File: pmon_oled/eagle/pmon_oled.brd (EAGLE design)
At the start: 60 x 60 mm, 37 parts, among them J1 USB, J2 USB, J4 PINHD-1X3, J5 PINHD-2X3, Q1 16Mhz, U1 LTC2943, U2 FT232RL, U3 LT1764AEQ, U4 ATMEGA328TQFP32

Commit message: Minor board tweaks. Ready for final auto routing.
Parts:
- moved J5 0.48 mm to (4.12, 26.7)
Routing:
- net +5V: track 160.2 -> 161.1 mm
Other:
- board text added: "(+)"
- board text added: "(-)"
- board text added: "(3.8V)"
- board text added: "+5V"
- board text added: "ICSP"
- board text added: "MODE"
- board text added: "POWER"
- board text added: "POWER-PLAY OLED - REV A OSH GITHUB"
- board text added: "POWER-PLAY OLED Rev A, May 2014 Single-Cell Power Monitor. Github OSH"
- board text added: "USB"
- board text added: "VOUT"
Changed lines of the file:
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@@
 <setting verticaltext="up"/>
 </settings>
-<grid distance="25" unitdist="mil" unit="mm" style="lines" multiple="1" display="yes" altdistance="0.000123031496" altunitdist="mil" altunit="mil"/>
+<grid distance="25" unitdist="mil" unit="mil" style="lines" multiple="1" display="yes" altdistance="0.000123031496" altunitdist="mil" altunit="mil"/>
 <layers>
 <layer number="1" name="Top" color="4" fill="1" visible="yes" active="yes"/>
@@
 <layer number="19" name="Unrouted" color="6" fill="1" visible="yes" active="yes"/>
 <layer number="20" name="Dimension" color="15" fill="1" visible="yes" active="yes"/>
-<layer number="21" name="tPlace" color="7" fill="1" visible="yes" active="yes"/>
+<layer number="21" name="tPlace" color="13" fill="1" visible="yes" active="yes"/>
 <layer number="22" name="bPlace" color="7" fill="1" visible="yes" active="yes"/>
 <layer number="23" name="tOrigins" color="15" fill="1" visible="yes" active="yes"/>
@@
 <circle x="56" y="56" radius="3" width="0.4064" layer="42"/>
 <circle x="56" y="4" radius="3" width="0.4064" layer="42"/>
+<text x="14.605" y="10.16" size="1.016" layer="21" font="vector" ratio="10" rot="SR0">POWER-PLAY OLED
+Rev A, May 2014
+Single-Cell
+Power Monitor.
+Github OSH</text>
+<wire x1="13.716" y1="18.034" x2="29.21" y2="18.034" width="0.1778" layer="21"/>
+<wire x1="29.21" y1="18.034" x2="29.21" y2="9.525" width="0.1778" layer="21"/>
+<wire x1="29.21" y1="9.525" x2="13.716" y2="9.525" width="0.1778" layer="21"/>
+<wire x1="13.716" y1="9.525" x2="13.716" y2="18.034" width="0.1778" layer="21"/>
+<text x="59.05229375" y="12.283228125" size="1.016" layer="21" ratio="10" rot="R90">VOUT</text>
+<text x="59.055" y="20.955" size="1.016" layer="21" ratio="10" rot="R90">(3.8V)</text>
+<text x="49.160525" y="1.87505625" size="1.016" layer="21" ratio="10" rot="R90">(+)</text>
+<text x="49.05901875" y="7.1835625" size="1.016" layer="21" ratio="10" rot="R90">(+)</text>
+<text x="49.113878125" y="4.4637625" size="1.016" layer="21" ratio="10" rot="R90">(-)</text>
+<text x="9.405546875" y="57.41788125" size="1.016" layer="21" ratio="10">USB</text>
+<text x="33.535546875" y="57.41788125" size="1.016" layer="21" ratio="10">+5V</text>
+<text x="28.94211875" y="50.680546875" size="1.016" layer="21" ratio="10" rot="R90">POWER</text>
+<text x="39.37433125" y="36.97023125" size="1.016" layer="21" ratio="10">MODE</text>
+<text x="2.54433125" y="21.09523125" size="1.016" layer="21" ratio="10" rot="SR0">ICSP</text>
+<text x="16.891" y="5.461" size="1.016" layer="30" font="vector" ratio="15" rot="SMR0" align="bottom-right">POWER-PLAY OLED - REV A
+OSH GITHUB</text>
 </plain>
 <attributes>
@@
 <param name="mdDrill" value="8mil"/>
 <param name="mdSmdStop" value="0mil"/>
-<param name="msWidth" value="8mil"/>
+<param name="msWidth" value="10mil"/>
 <param name="msDrill" value="13mil"/>
 <param name="msMicroVia" value="9.99mm"/>
@@
 <attribute name="NAME" x="4.70601875" y="38.33854375" size="1.016" layer="25" font="vector" ratio="10"/>
 </element>
-<element name="J5" library="pmon_oled" package="2X03" value="PINHD-2X3" x="4.125" y="26.19" smashed="yes" rot="R90">
-<attribute name="NAME" x="3.41003125" y="30.43926875" size="1.016" layer="25" font="vector" ratio="10"/>
+<element name="J5" library="pmon_oled" package="2X03" value="PINHD-2X3" x="4.125" y="26.67" smashed="yes" rot="R90">
+<attribute name="NAME" x="3.41003125" y="30.91926875" size="1.016" layer="25" font="vector" ratio="10"/>
 </element>
 <element name="R10" library="pmon_oled" package="R0603" value="10K" x="22.225" y="47.625" smashed="yes" rot="R180">
@@
 </element>
 <element name="R9" library="pmon_oled" package="R0603" value="3K3 1%" x="56.388" y="22.86" smashed="yes" rot="R180">
-<attribute name="NAME" x="56.157925" y="24.374953125" size="1.016" layer="25" font="vector" ratio="10"/>
+<attribute name="NAME" x="54.0102875" y="24.18703125" size="1.016" layer="25" font="vector" ratio="10"/>
 </element>
 <element name="C8" library="pmon_oled" package="A/3216-18R" value="10uF" x="49.149" y="21.717" smashed="yes">
@@
 </element>
 <element name="U2" library="pmon_oled" package="SSOP28DB" value="FT232RL" x="7.065" y="44.69" smashed="yes">
-<attribute name="NAME" x="1.325009375" y="38.3318625" size="1.016" layer="25" font="vector" ratio="10"/>
+<attribute name="NAME" x="1.960009375" y="49.7618625" size="1.016" layer="25" font="vector" ratio="10"/>
 </element>
 <element name="S1" library="pmon_oled" package="TLE1105" value="PUSH_BUTTON_SHIELDED" x="4.205" y="16.745" smashed="yes" rot="R180">
@@
 </element>
 <element name="J4" library="pmon_oled" package="1X03" value="PINHD-1X3" x="46.435" y="5.475" smashed="yes" rot="R90">
-<attribute name="NAME" x="49.84005" y="8.98095" size="1.016" layer="25" font="vector" ratio="10" rot="R180"/>
+<attribute name="NAME" x="47.536246875" y="10.73651875" size="1.016" layer="25" font="vector" ratio="10" rot="R180"/>
 </element>
 <element name="OLED" library="pmon_oled" package="OLED" value="OLED" x="19.44" y="31.51" smashed="yes">
@@
 <wire x1="21.98" y1="31.51" x2="21.9964" y2="31.4936" width="0.508" layer="1"/>
 <wire x1="21.9964" y1="31.4936" x2="21.9964" y2="26.67" width="0.508" layer="1"/>
-<wire x1="19.05" y1="26.67" x2="21.9964" y2="26.67" width="0.508" layer="1"/>
-<wire x1="22.86" y1="26.67" x2="34.925" y2="26.67" width="0.508" layer="1"/>
-<wire x1="2.855" y1="23.65" x2="4.915" y2="21.59" width="0.508" layer="1"/>
-<wire x1="4.915" y1="21.59" x2="13.97" y2="21.59" width="0.508" layer="1"/>
-<wire x1="13.97" y1="21.59" x2="19.05" y2="26.67" width="0.508" layer="1"/>
-<wire x1="21.9964" y1="26.67" x2="22.86" y2="26.67" width="0.508" layer="1"/>
+<wire x1="21.9964" y1="26.67" x2="34.925" y2="26.67" width="0.508" layer="1"/>
+<wire x1="2.855" y1="24.13" x2="2.855" y2="22.545" width="0.508" layer="1"/>
+<wire x1="2.855" y1="22.545" x2="3.60135" y2="21.79865" width="0.508" layer="1"/>
+<wire x1="3.60135" y1="21.79865" x2="7.735890625" y2="21.79865" width="0.508" layer="1"/>
+<wire x1="7.735890625" y1="21.79865" x2="12.607240625" y2="26.67" width="0.508" layer="1"/>
+<wire x1="12.607240625" y1="26.67" x2="21.9964" y2="26.67" width="0.508" layer="1"/>
 <wire x1="33.655" y1="38.735" x2="32.385" y2="38.735" width="0" layer="19" extent="1-1"/>
 </signal>
@@
 <wire x1="24.92" y1="46.415" x2="24.92" y2="45.0126" width="0.254" layer="1"/>
 <wire x1="10.2108" y1="36.91" x2="23.075" y2="47.625" width="0" layer="19" extent="1-1"/>
-<wire x1="5.395" y1="28.73" x2="10.2108" y2="36.91" width="0" layer="19" extent="1-1"/>
+<wire x1="5.395" y1="29.21" x2="10.2108" y2="36.91" width="0" layer="19" extent="1-1"/>
 </signal>
 <signal name="N$17">
@@
 <wire x1="29.718" y1="37.846" x2="29.6126" y2="37.92" width="0.254" layer="1"/>
 <wire x1="24.52" y1="31.51" x2="29.6126" y2="37.92" width="0" layer="19" extent="1-1"/>
-<wire x1="5.395" y1="26.19" x2="24.52" y2="31.51" width="0" layer="19" extent="1-1"/>
+<wire x1="5.395" y1="26.67" x2="24.52" y2="31.51" width="0" layer="19" extent="1-1"/>
 </signal>
 <signal name="SER_RX">
@@
 <contactref element="C7" pad="1"/>
 <contactref element="U2" pad="17"/>
-<wire x1="14.605" y1="46.57" x2="13.55" y2="46.355" width="0" layer="19" extent="1-16"/>
 <wire x1="9.99" y1="47.16" x2="9.99" y2="48.346" width="0.254" layer="1"/>
 <wire x1="9.99" y1="47.16" x2="10.58" y2="46.57" width="0.254" layer="1"/>
@@
 <contactref element="OLED" pad="4"/>
 <wire x1="27.06" y1="31.51" x2="27.32" y2="36.4274" width="0" layer="19" extent="1-1"/>
-<wire x1="2.855" y1="26.19" x2="27.06" y2="31.51" width="0" layer="19" extent="1-1"/>
+<wire x1="2.855" y1="26.67" x2="27.06" y2="31.51" width="0" layer="19" extent="1-1"/>
 </signal>
 <signal name="SENSE+">
@@
 <contactref element="U4" pad="16"/>
 <contactref element="J5" pad="1"/>
-<wire x1="5.395" y1="23.65" x2="28.12" y2="36.4274" width="0" layer="19" extent="1-1"/>
+<wire x1="5.395" y1="24.13" x2="28.12" y2="36.4274" width="0" layer="19" extent="1-1"/>
 </signal>
 <signal name="VUSB">
@@
 </board>
 </drawing>
+<compatibility>
+<note version="6.3" minversion="6.2.2" severity="warning">
+Since Version 6.2.2 text objects can contain more than one line,
+which will not be processed correctly with this version.
+</note>
+</compatibility>
 </eagle>

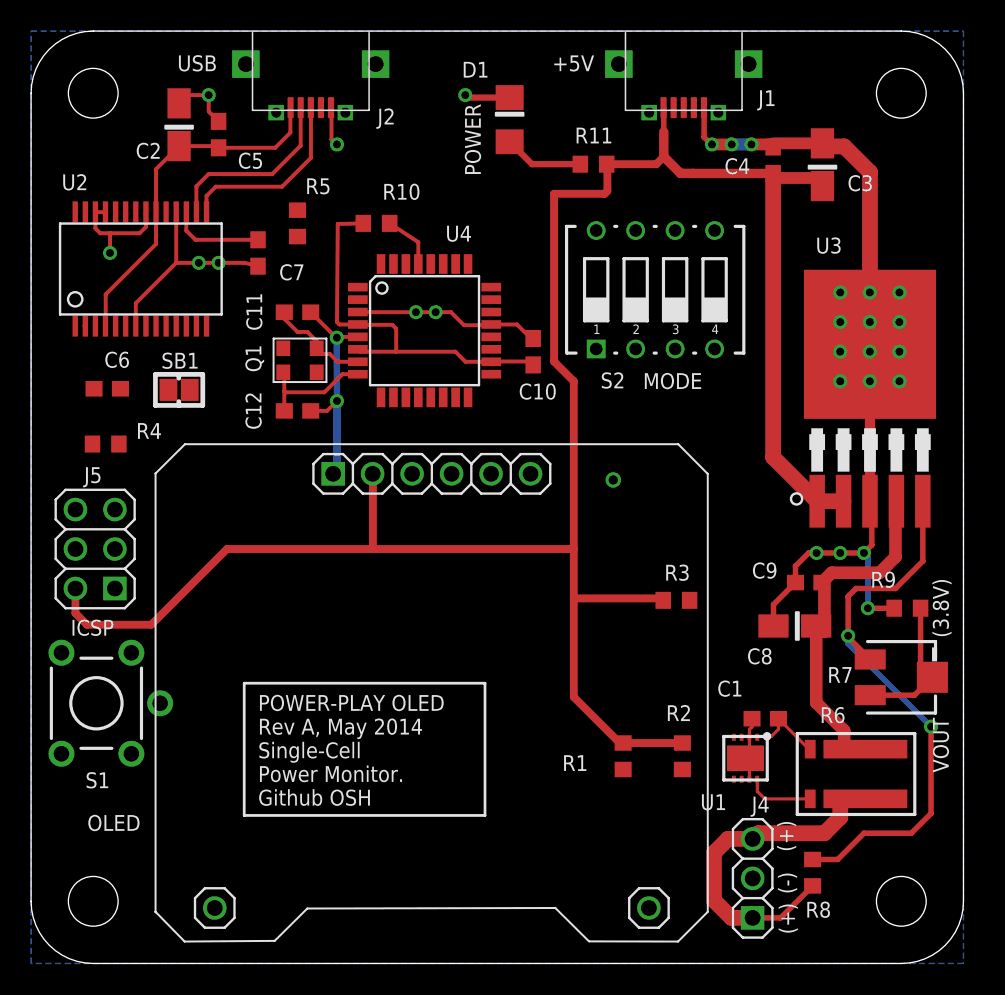
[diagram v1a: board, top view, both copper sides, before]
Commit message: Updated the layout for physical clearance.
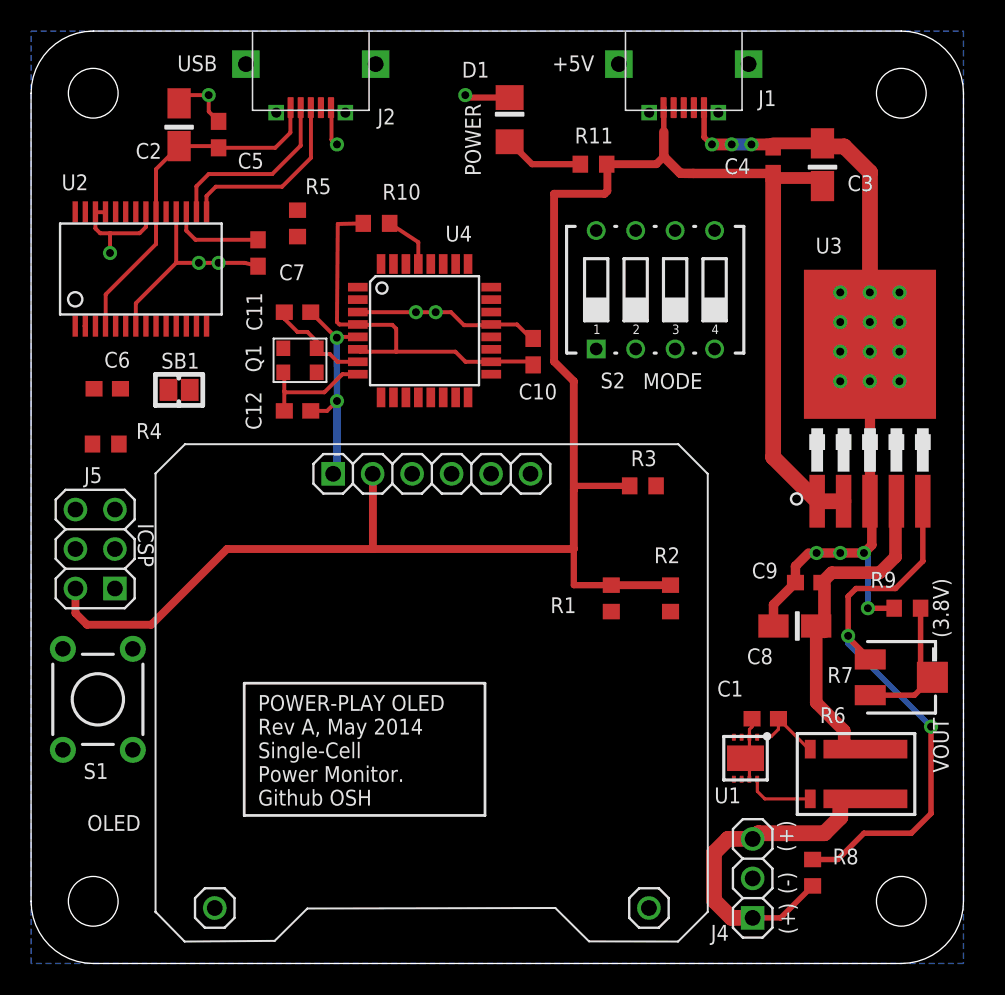
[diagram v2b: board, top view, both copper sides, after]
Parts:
- S1: value PUSH_BUTTON_SHIELDED -> PUSH_BUTTON
- moved R1 10.2 mm to (37.3, 23.5)
- moved R2 10.2 mm to (41.1, 23.5)
- moved R3 7.68 mm to (39.4, 30.7)
- moved S1 0.27 mm to (4.30, 17.0), turned to 0 degrees
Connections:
- net GND: no longer S1.G
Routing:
- net +5V: track 161.1 -> 150.0 mm
- net GND: vias 30 -> 29
